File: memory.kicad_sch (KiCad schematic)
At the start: 29 parts, among them U10 TPS2117DRLR, U2 SDINBDG4-8G, U9 TPS2117DRLR

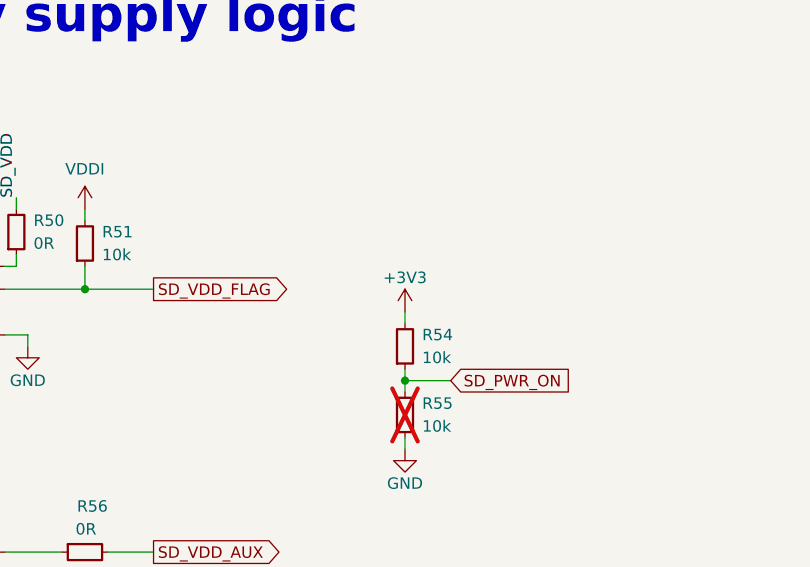
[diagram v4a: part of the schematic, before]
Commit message: [#57970] Update SD connection
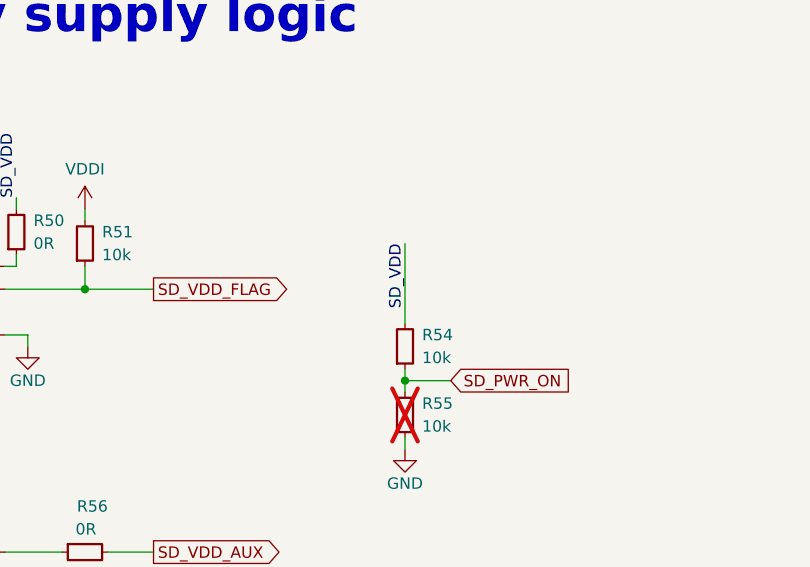
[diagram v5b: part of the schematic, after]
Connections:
- net +3V3: no longer R54.2
- net SD_VDD: now also R54.2
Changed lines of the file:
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@@
     (stroke (width 0) (type default))
   )
-  (wire (pts (xy 128.27 205.74) (xy 128.27 207.01))
+  (wire (pts (xy 128.27 198.12) (xy 128.27 207.01))
     (stroke (width 0) (type default))
   )
@@
     (effects (font (size 1.27 1.27)) (justify right bottom))
   )
+  (label "SD_VDD" (at 128.27 198.12 270) (fields_autoplaced)
+    (effects (font (size 1.27 1.27)) (justify right bottom))
+  )
   (label "SD_VDD" (at 191.77 93.98 0) (fields_autoplaced)
     (effects (font (size 1.27 1.27)) (justify left bottom))
@@
         )
       )
-    )
-  )
-  (symbol (lib_id "antmicropower:+3V3") (at 128.27 205.74 0) (unit 1)
-    (in_bom yes) (on_board yes) (dnp no)
-    (property "Reference" "#PWR0195" (at 143.51 208.28 0)
-      (effects (font (size 1.27 1.27) (thickness 0.15)) (justify left bottom) hide)
-    )
-    (property "Value" "+3V3" (at 128.27 201.93 0)
-      (effects (font (size 1.27 1.27) (thickness 0.15)))
-    )
-    (property "Footprint" "" (at 143.51 213.36 0)
-      (effects (font (size 1.27 1.27) (thickness 0.15)) (justify left bottom) hide)
-    )
-    (property "Datasheet" "" (at 143.51 215.9 0)
-      (effects (font (size 1.27 1.27) (thickness 0.15)) (justify left bottom) hide)
-    )
-    (property "Author" "Antmicro" (at 143.51 213.36 0)
-      (effects (font (size 1.27 1.27) (thickness 0.15)) (justify left bottom) hide)
-    )
-    (property "License" "Apache-2.0" (at 143.51 215.9 0)
-      (effects (font (size 1.27 1.27) (thickness 0.15)) (justify left bottom) hide)
-    )
-    (pin "1")
-    (instances
-      (project "polarfire-som"
-        (path "/db4a0d3e-2eb3-499e-977d-6eb378cfd3ed/6b5c9386-08fc-46bf-a582-c320c1d104da"
-          (reference "#PWR0195") (unit 1)
-        )
-      )
